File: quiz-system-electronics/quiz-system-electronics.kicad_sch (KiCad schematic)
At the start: 25 parts, among them U1 74HC595, U2 74HC595, U3 74HC595, U4 ULN2803A, U5 ULN2803A

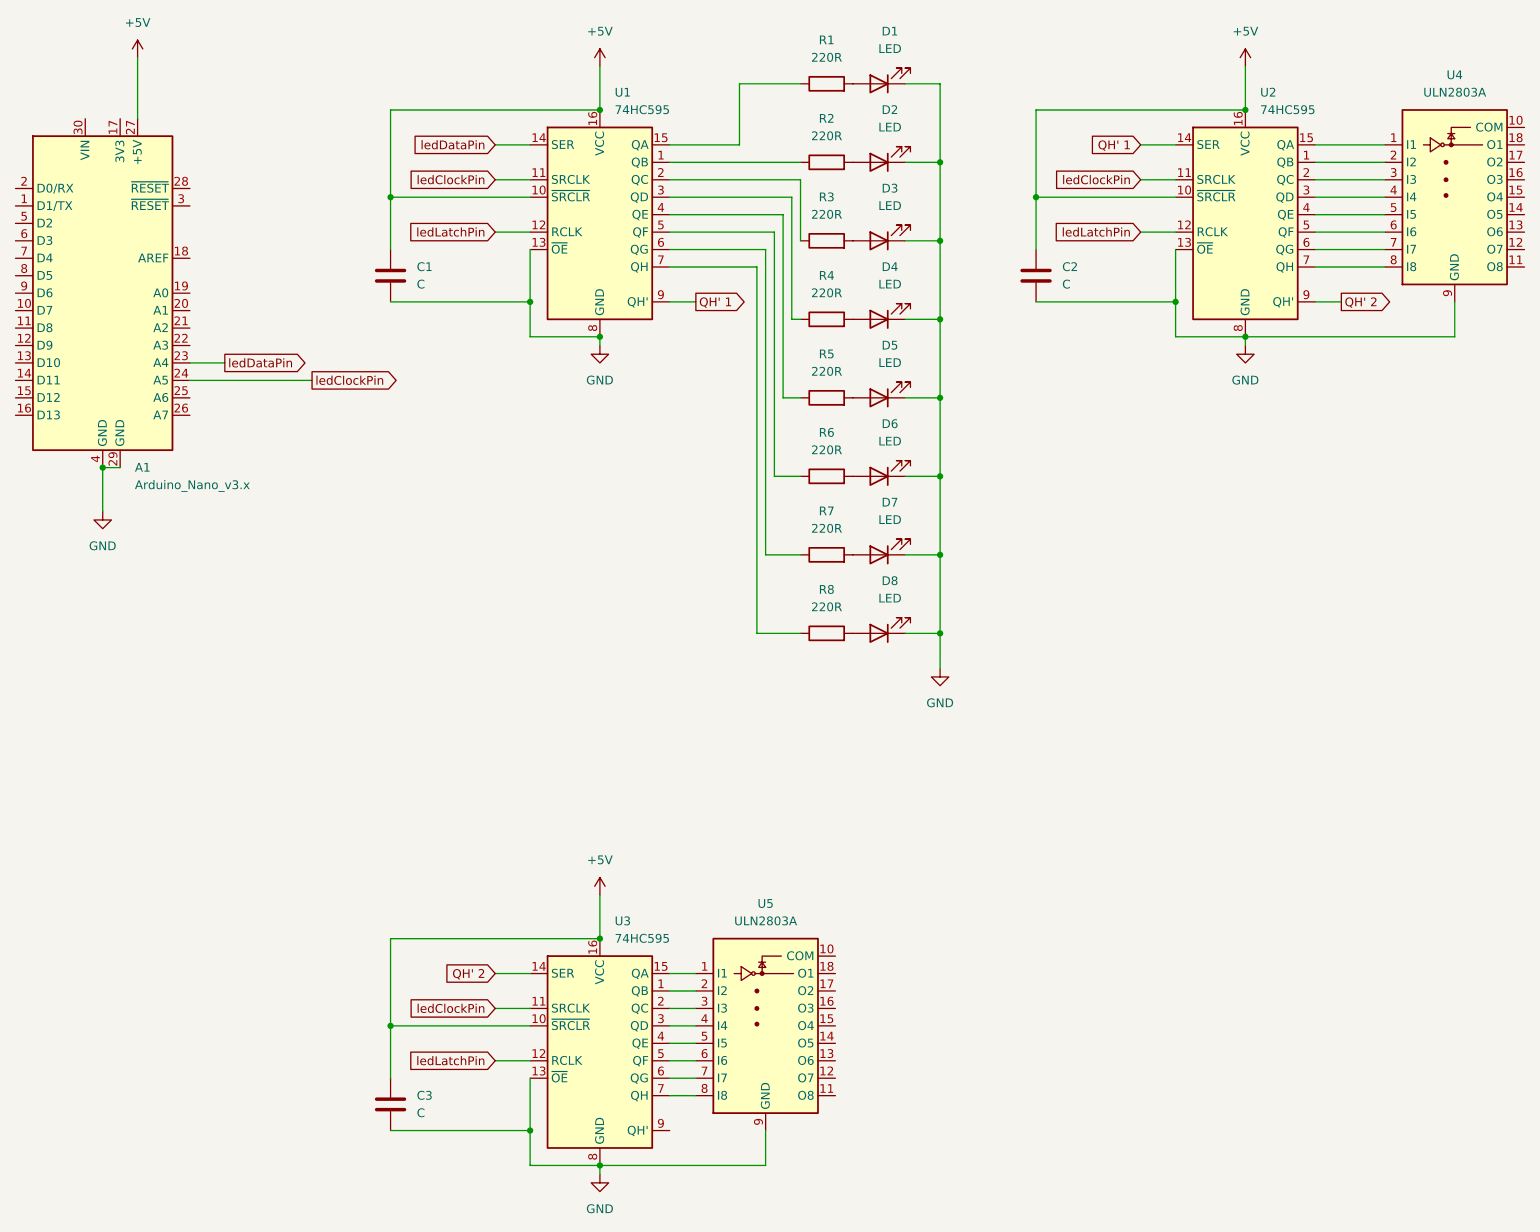
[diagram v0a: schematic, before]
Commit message: Updated schematic and started to connect PCB
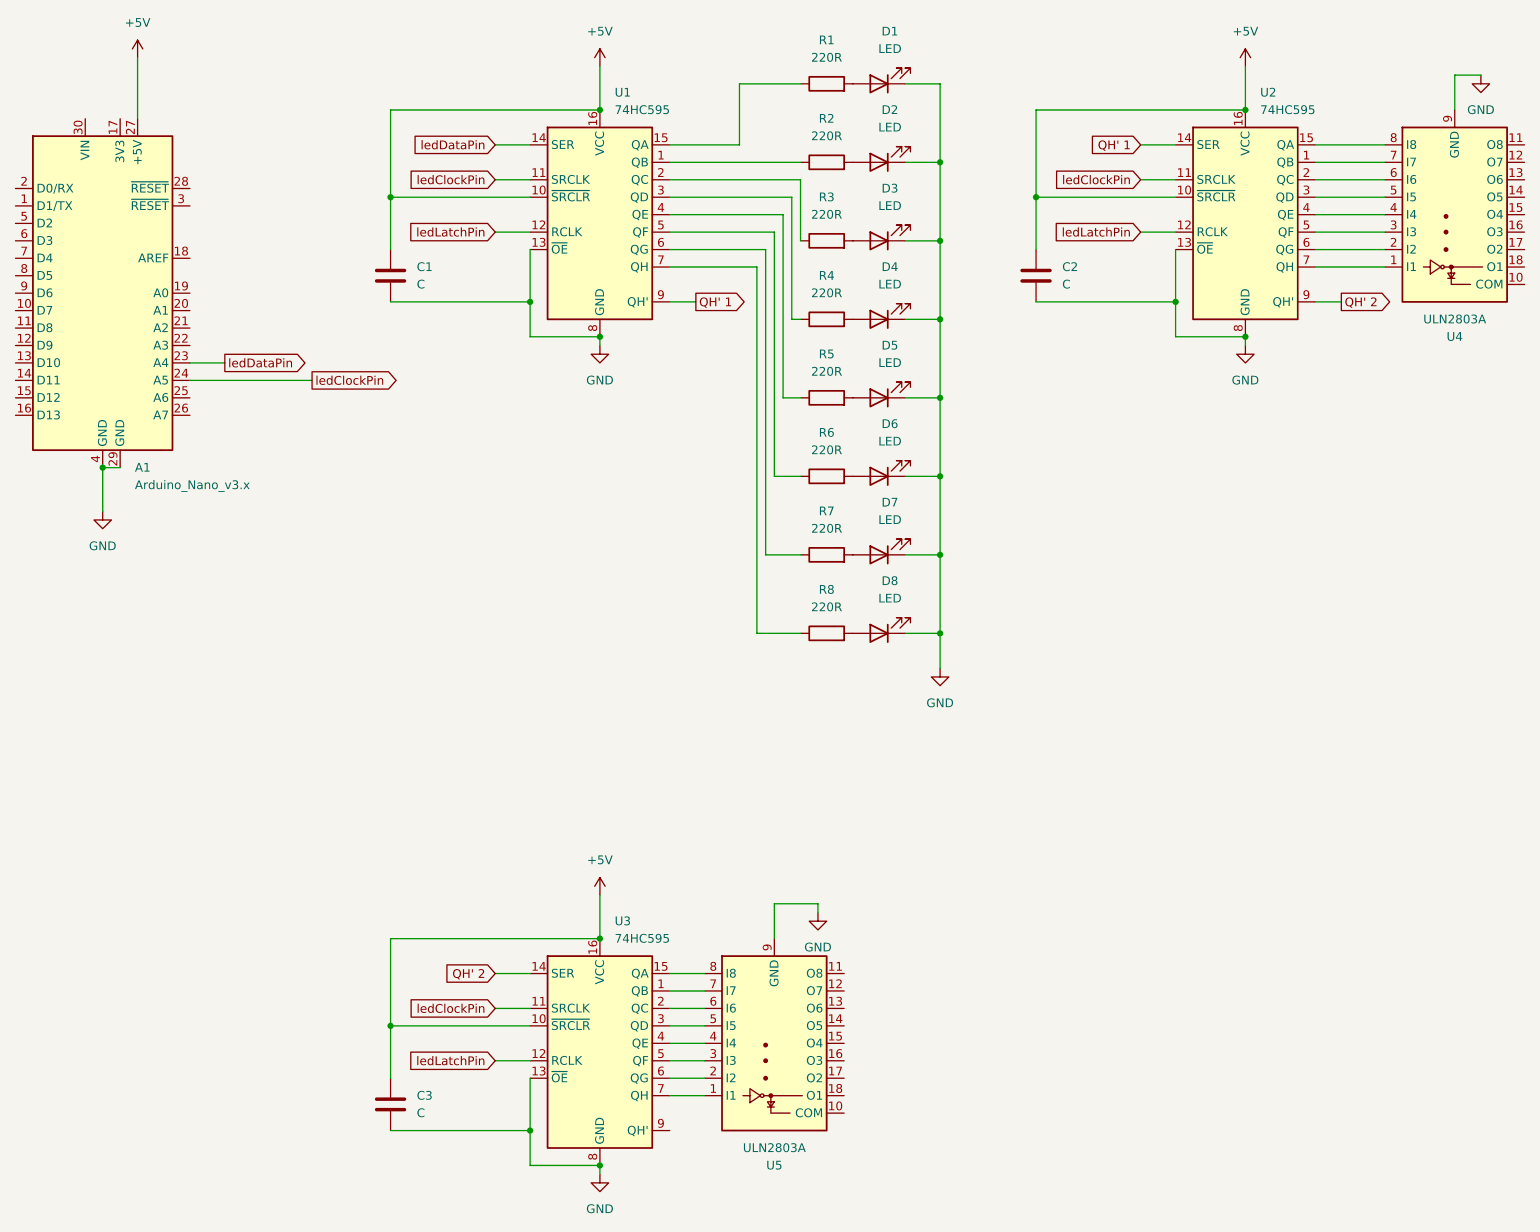
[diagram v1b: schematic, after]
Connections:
- net at U4.1 (I1): now also U2.7 (QH); no longer U2.15 (QA)
- net at U4.2 (I2): now also U2.6 (QG); no longer U2.1 (QB)
- net at U4.3 (I3): now also U2.5 (QF); no longer U2.2 (QC)
- net at U4.4 (I4): now also U2.4 (QE); no longer U2.3 (QD)
- net at U4.5 (I5): now also U2.3 (QD); no longer U2.4 (QE)
- net at U4.6 (I6): now also U2.2 (QC); no longer U2.5 (QF)
- net at U4.7 (I7): now also U2.1 (QB); no longer U2.6 (QG)
- net at U4.8 (I8): now also U2.15 (QA); no longer U2.7 (QH)
- net at U3.1 (QB): now also U5.7 (I7); no longer U5.2 (I2)
- net at U3.15 (QA): now also U5.8 (I8); no longer U5.1 (I1)
- net at U3.2 (QC): now also U5.6 (I6); no longer U5.3 (I3)
- net at U3.3 (QD): now also U5.5 (I5); no longer U5.4 (I4)
- net at U3.4 (QE): now also U5.4 (I4); no longer U5.5 (I5)
- net at U3.5 (QF): now also U5.3 (I3); no longer U5.6 (I6)
- net at U3.6 (QG): now also U5.2 (I2); no longer U5.7 (I7)
- net at U3.7 (QH): now also U5.1 (I1); no longer U5.8 (I8)
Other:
- moved on the sheet: U5
